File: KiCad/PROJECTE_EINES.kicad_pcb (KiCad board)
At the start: 2 copper layers, 107 x 101.9 mm, 67 parts, among them J1 Conn_01x08_Pin, J2 DE9_Pins_MountingHoles, SW1 SS-1GL2-F-D, U1 VNH5019A-E, U2 VNH5019A-E, U3 LM2596S-5, U4 SN65HVD230, U5 LM1117DT-3.3, U7 PIC24HJ128GP504-I_PT, Y1 8MHz

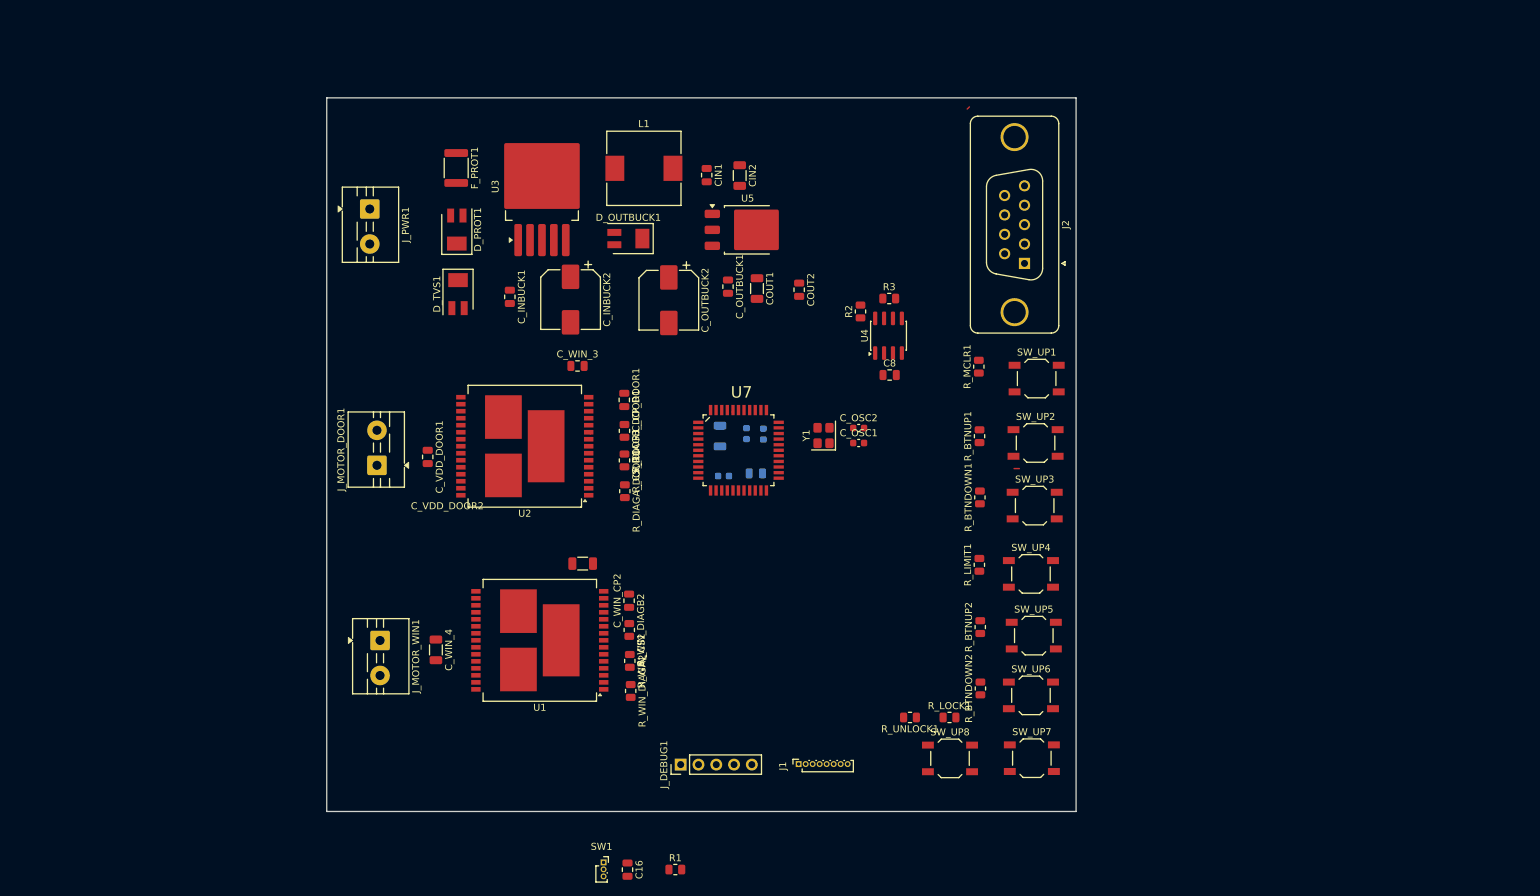
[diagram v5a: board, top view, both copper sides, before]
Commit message: Actulitació de components
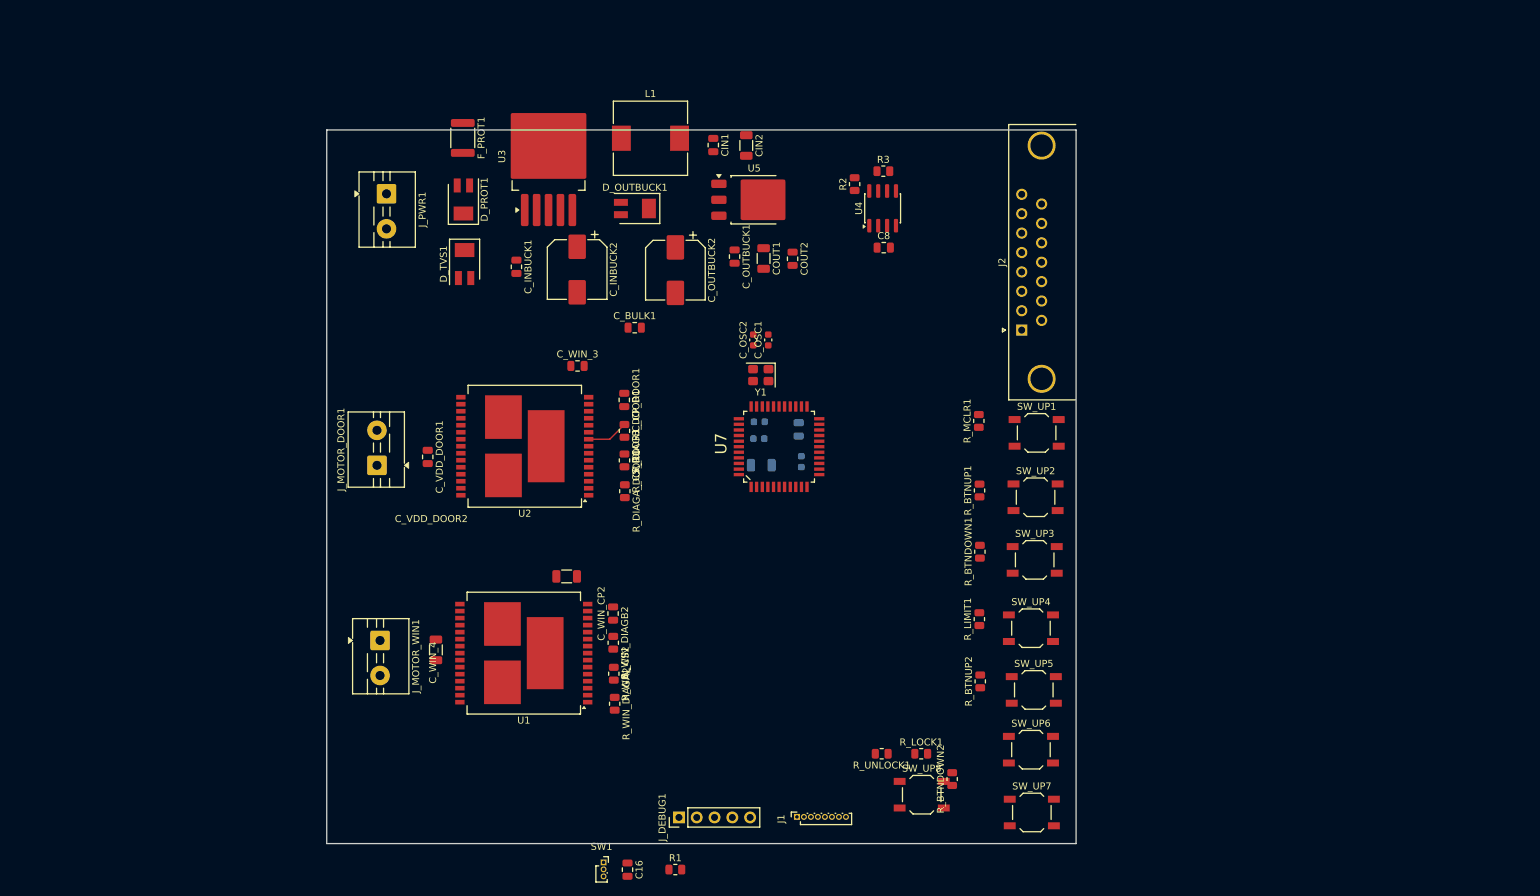
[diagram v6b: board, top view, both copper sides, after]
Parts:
- added C_BULK1: 10uF, Capacitor_SMD:C_0805_2012Metric, F.Cu at (105.7, 64.8)
- J2: footprint Connector_Dsub:DSUB-9_Socket_Vertical_P2.77x2.84mm_MountingHoles -> Connector_Dsub:DSUB-15_Pins_Horizontal_P2.77x2.84mm_EdgePinOffset4.94mm_Housed_MountingHolesOffset4.94mm
- moved C_OSC2 19.6 mm to (122.7, 66.5), turned to 90 degrees
- moved C_OSC1 19.6 mm to (124.8, 66.5), turned to 90 degrees
- moved R2 18.2 mm to (137.1, 44.3)
- moved R3 18.2 mm to (141.2, 42.4)
- moved U4 18.2 mm to (141.1, 47.7)
- moved C8 18.2 mm to (141.3, 53.3)
- moved R_BTNDOWN2 13.5 mm to (151.1, 129.2)
- moved Y1 12.4 mm to (123.7, 71.5), turned to 180 degrees
- moved C_AVDD1 11.3 mm to (129.5, 83.9), turned to -90 degrees
- moved J2 9.53 mm to (161.0, 65.1), turned to 90 degrees
- moved C1 8.77 mm to (129.1, 79.3), turned to -90 degrees
- moved R_BTNDOWN1 7.75 mm to (155.0, 96.8)
- moved R_BTNUP2 7.75 mm to (155.1, 115.3)
- moved SW_UP4 7.75 mm to (162.3, 107.7)
- moved SW_UP5 7.75 mm to (162.7, 116.5)
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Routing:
- net DOOR_DIAGB: track 0.00 -> 5.98 mm
- net UART_RX: track 1.22 -> 0.00 mm

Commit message: V2 placement
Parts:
- removed R_BTNDOWN2, R_BTNUP2, R_LIMIT1, R_LOCK1, R_UNLOCK1: 10K, Resistor_SMD:R_0805_2012Metric
- removed SW_UP2, SW_UP5: SW_WINUP, Button_Switch_SMD:SW_SPST_TL3342
- removed SW_UP3, SW_UP6: SW_WINDOWN, Button_Switch_SMD:SW_SPST_TL3342
- removed SW_UP4, SW_UP7, SW_UP8: SW_LIMIT, Button_Switch_SMD:SW_SPST_TL3342
- removed the U4 at (141.1, 47.7)
- added C2: 100nF, Capacitor_SMD:C_0805_2012Metric, F.Cu at (204.2, 125.3)
- added J1: DE9_Pins_MountingHoles, Connector_Dsub:DSUB-15_Socket_Horizontal_P2.77x2.84mm_EdgePinOffset4.94mm_Housed_MountingHolesOffset4.94mm, F.Cu at (176.6, 66.2)
- added R4: 10k, Resistor_SMD:R_0805_2012Metric, F.Cu at (208.6, 125.2)
- added R_Lock/Unlock1: 10K, Resistor_SMD:R_0805_2012Metric, F.Cu at (177.6, 128.5)
- added SW2: SW_DPDT_x2, Button_Switch_SMD:SW_DPDT_CK_JS202011JCQN, F.Cu at (194.7, 121.0)
- added SW3: SW_DPDT_x2, Button_Switch_SMD:SW_DPDT_CK_JS202011JCQN, F.Cu at (207.2, 121.0)
- added SW4: SW_DPDT_x2, Button_Switch_SMD:SW_DPDT_CK_JS202011JCQN, F.Cu at (194.7, 126.5)
- added U2: SN65HVD230, Package_SO:SOIC-8_3.9x4.9mm_P1.27mm, F.Cu at (143.0, 47.9)
- C_OUTBUCK2: value 220uF -> 100uF
- J2: footprint Connector_Dsub:DSUB-15_Pins_Horizontal_P2.77x2.84mm_EdgePinOffset4.94mm_Housed_MountingHolesOffset4.94mm -> Connector_Dsub:DSUB-15_Socket_Horizontal_P2.77x2.84mm_EdgePinOffset4.94mm_Housed_MountingHolesOffset4.94mm
- R_DIAGA_DOOR1, R_DIAGB_DOOR1: value 3.3k -> 10K
- R_WIN_CS1: renamed from R_WIN_CS2; value 1,5K -> 1K
- R_WIN_DIAGA1: renamed from R_WIN_DIAGA2; value 3.3k -> 10K
- R_WIN_DIAGB1: renamed from R_WIN_DIAGB2; value 3.3k -> 10K
- moved SW_UP1 69.5 mm to (203.4, 136.4)
- moved R_MCLR1 58.1 mm to (177.6, 131.5), turned to 0 degrees
- moved J2 45.5 mm to (176.9, 107.7), turned to -90 degrees
- moved R_BTNUP1 41.4 mm to (177.6, 122.6), turned to 0 degrees
- moved R_BTNDOWN1 32.2 mm to (177.6, 119.7), turned to 0 degrees
- renumbered C8 to C1, C1 to C3, CIN2 to CIN1, C_WIN_3 to C_WIN_1, C_WIN_4 to C_WIN_2, C_WIN_CP2 to C_WIN_CP1, J1 to J3, U7 to U1, U1 to U3, U3 to U4, U2 to U5, U5 to U6
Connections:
- net VBAT_12V renamed +12V
- C1 pad 2: VDD_3V3 -> +3.3V
- COUT1 pad 1: VDD_3V3 -> +3.3V
- COUT2 pad 1: VDD_3V3 -> +3.3V
- C_AVDD1 pad 1: VDD_3V3 -> +3.3V
- C_BULK1 pad 1: VDD_3V3 -> +3.3V
- C_VDD1 pad 1: VDD_3V3 -> +3.3V
- C_VDD2 pad 1: VDD_3V3 -> +3.3V
- J2 pad 1: GND -> unconnected-(J2-Pad1)
- J2 pad 2: unconnected-(J2-Pad2) -> UART_RX
- J2 pad 3: /COMUNICACIONS/CANH -> UART_TX
- J2 pad 5: UART_TX -> GND
- J2 pad 7: /COMUNICACIONS/CANL -> unconnected-(J2-Pad7)
- J2 pad 9: UART_RX -> unconnected-(J2-Pad9)
- J3 pad 6: VDD_3V3 -> WIN_LIMIT
- J_DEBUG1 pad 2: VDD_3V3 -> +3.3V
- R_BTNDOWN1 pad 1: VDD_3V3 -> WIN_BTN_DOWN
- R_BTNDOWN1 pad 2: WIN_BTN_DOWN -> GND
- R_BTNUP1 pad 1: VDD_3V3 -> WIN_BTN_UP
- R_BTNUP1 pad 2: WIN_BTN_UP -> GND
- R_DIAGA_DOOR1 pad 2: VDD_3V3 -> +3.3V
- R_DIAGB_DOOR1 pad 2: VDD_3V3 -> +3.3V
- R_MCLR1 pad 1: VDD_3V3 -> +3.3V
- R_WIN_DIAGA1 pad 2: VDD_3V3 -> +3.3V
- R_WIN_DIAGB1 pad 2: VDD_3V3 -> +3.3V
- U1 pad 12: DOOR_UNLOCK_SW -> DOOR_LOCK/UNLOCK
- U1 pad 13: DOOR_BTN_OPEN -> unconnected-(U1-TCK/PMA7/RA7-Pad13)
- U1 pad 17: VDD_3V3 -> +3.3V
- U1 pad 28: VDD_3V3 -> +3.3V
- U1 pad 32: DOOR_BTN_CLOSED -> unconnected-(U1-TDO/PMA8/RA8-Pad32)
- U1 pad 35: DOOR_LOCK_SW -> unconnected-(U1-TDI/PMA9/RA9-Pad35)
- U1 pad 4: DOOR_LIMIT_OPEN -> unconnected-(U1-RP24(1)/CN20/PMA5/RC8-Pad4)
- U1 pad 40: VDD_3V3 -> +3.3V
- U1 pad 5: DOOR_LIMIT_CLOSE -> unconnected-(U1-RP25(1)/CN19/PMA6/RC9-Pad5)
- U3 pad 6: GND -> GNDPWR
- U5 pad 6: VDD_3V3 -> GNDPWR
- U6 pad 2: VDD_3V3 -> +3.3V

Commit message: Update
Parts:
- moved R_BTNDOWN1 56.5 mm to (122.5, 107.2)
- moved R_BTNUP1 56.5 mm to (122.5, 110.2)
- moved R_Lock/Unlock1 56.5 mm to (122.5, 116.1)
- moved R_MCLR1 56.5 mm to (122.5, 119.0)
- moved C2 56.5 mm to (149.0, 112.8)
- moved R4 56.5 mm to (153.5, 112.8)
- moved SW2 56.5 mm to (139.5, 108.5)
- moved SW3 56.5 mm to (152.1, 108.5)
- moved SW4 56.5 mm to (139.5, 114.1)
- moved SW_UP1 56.5 mm to (148.2, 124.0)
- moved J2 23.2 mm to (164.5, 88.1), turned to 90 degrees
- moved J1 22.9 mm to (164.5, 46.8), turned to 90 degrees
- moved CIN1 4.00 mm to (118.3, 42.5)
- moved CIN1 4.00 mm to (123.0, 42.5)
- moved COUT1 4.00 mm to (125.4, 58.7)
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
